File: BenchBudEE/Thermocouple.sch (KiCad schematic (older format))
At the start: 28 parts, among them P2 CONN_3X2, P3 CONN_2, U2 MCP3901, U3 LMT84, U4 OPA4170

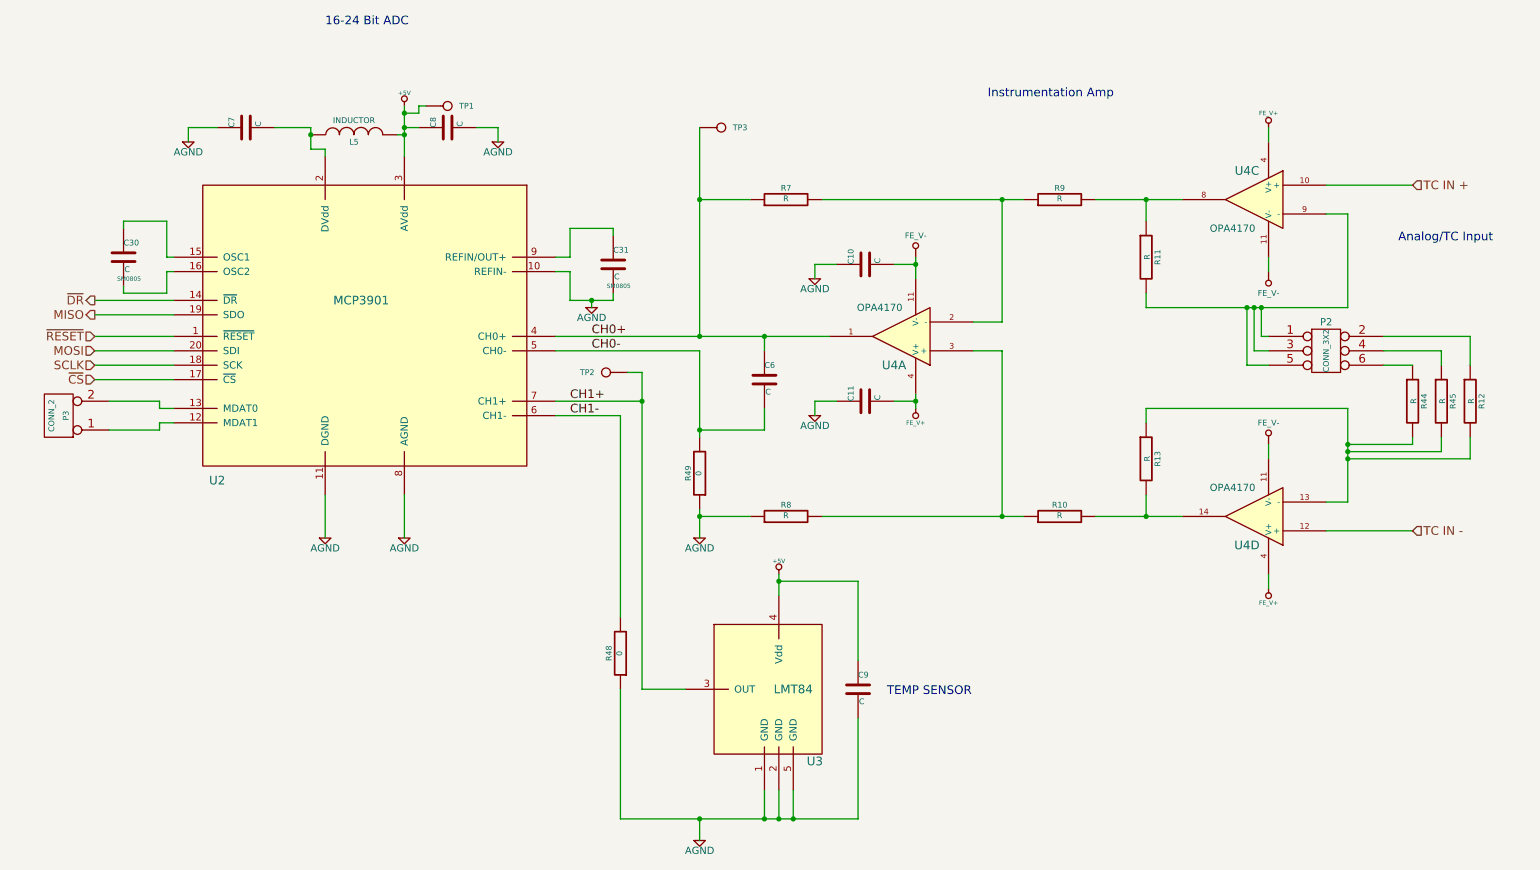
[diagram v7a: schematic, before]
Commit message: Analog IO Cleanup/Additions
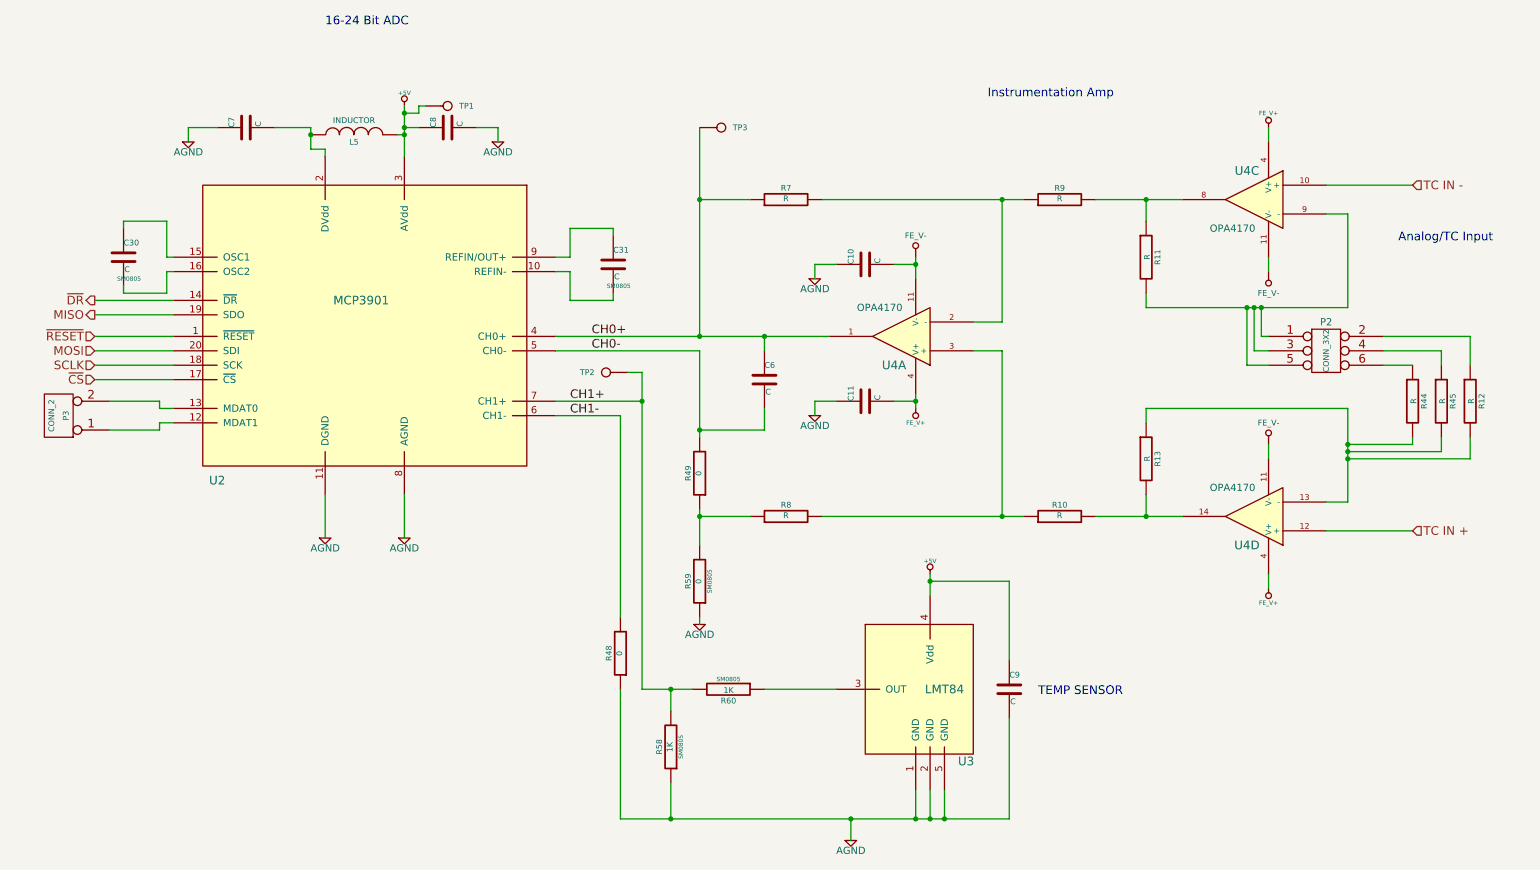
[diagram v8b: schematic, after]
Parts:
- added R58, R60: 1K, SM0805, symbol R
- added R59: 0, SM0805, symbol R
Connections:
- net AGND: now also R58.1, R59.1; no longer C31.2, R49.1, R8.1, U2.10 (REFIN-)
- net CH1+: now also R58.2, R60.2; no longer U3.3 (OUT)
- net TC IN +: now also U4.12 (+); no longer U4.10 (+)
- net TC IN -: now also U4.10 (+); no longer U4.12 (+)
- new net: R49.1, R59.2, R8.1
- new net: C31.2, U2.10 (REFIN-)
- new net: R60.1, U3.3 (OUT)
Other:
- moved on the sheet: C9, U3
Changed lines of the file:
@@
 Sheet 2 9
 Title ""
-Date "20 mar 2014"
+Date "26 mar 2014"
 Rev ""
 Comp ""
@@
 $EndDescr
 Text HLabel 10200 2100 2    60   Input ~ 0
+TC IN -
+Text HLabel 10200 4500 2    60   Input ~ 0
 TC IN +
-Text HLabel 10200 4500 2    60   Input ~ 0
-TC IN -
 Text HLabel 1050 3250 0    60   Input ~ 0
 MOSI
@@
 L LMT84 U3
 U 1 1 5303AA1C
-P 5700 5650
-F 0 "U3" H 6050 5200 60  0000 C CNN
-F 1 "LMT84" H 5900 5700 60  0000 C CNN
-F 2 "" H 6000 5500 60  0000 C CNN
-F 3 "" H 6000 5500 60  0000 C CNN
-	1    5700 5650
-	1    0    0    -1
-$EndComp
-$Comp
-L +5V #PWR9
+P 6750 5650
+F 0 "U3" H 7100 5200 60  0000 C CNN
+F 1 "LMT84" H 6950 5700 60  0000 C CNN
+F 2 "" H 7050 5500 60  0000 C CNN
+F 3 "" H 7050 5500 60  0000 C CNN
+	1    6750 5650
+	1    0    0    -1
+$EndComp
+$Comp
+L +5V #PWR01
 U 1 1 5303ACCB
-P 5800 4800
-F 0 "#PWR9" H 5800 4890 20  0001 C CNN
-F 1 "+5V" H 5800 4890 30  0000 C CNN
-F 2 "" H 5800 4800 60  0000 C CNN
-F 3 "" H 5800 4800 60  0000 C CNN
-	1    5800 4800
+P 6850 4800
+F 0 "#PWR01" H 6850 4890 20  0001 C CNN
+F 1 "+5V" H 6850 4890 30  0000 C CNN
+F 2 "" H 6850 4800 60  0000 C CNN
+F 3 "" H 6850 4800 60  0000 C CNN
+	1    6850 4800
 	1    0    0    -1
 $EndComp
@@
 L C C9
 U 1 1 5303AD83
-P 6350 5600
-F 0 "C9" H 6350 5700 40  0000 L CNN
-F 1 "C" H 6356 5515 40  0000 L CNN
-F 2 "~" H 6388 5450 30  0000 C CNN
-F 3 "~" H 6350 5600 60  0000 C CNN
-	1    6350 5600
+P 7400 5600
+F 0 "C9" H 7400 5700 40  0000 L CNN
+F 1 "C" H 7406 5515 40  0000 L CNN
+F 2 "~" H 7438 5450 30  0000 C CNN
+F 3 "~" H 7400 5600 60  0000 C CNN
+	1    7400 5600
 	1    0    0    -1
 $EndComp
@@
 $EndComp
 $Comp
-L +5V #PWR3
+L +5V #PWR02
 U 1 1 5303B53D
 P 3200 1550
-F 0 "#PWR3" H 3200 1640 20  0001 C CNN
+F 0 "#PWR02" H 3200 1640 20  0001 C CNN
 F 1 "+5V" H 3200 1640 30  0000 C CNN
 F 2 "" H 3200 1550 60  0000 C CNN
@@
 	0    -1   -1   0
 $EndComp
-Text Notes 6550 5650 0    60   ~ 0
+Text Notes 7600 5650 0    60   ~ 0
 TEMP SENSOR
 Text HLabel 1050 3150 0    60   Input ~ 0
@@
 Connection ~ 5250 4400
 Wire Wire Line
-	5250 6500 5250 6650
+	6300 6500 6300 6650
 Wire Wire Line
 	4250 3250 5250 3250
@@
 	4850 3400 4850 5600
 Wire Wire Line
-	4850 5600 5150 5600
-Wire Wire Line
 	4700 3700 4250 3700
 Wire Wire Line
-	4700 6500 6350 6500
-Wire Wire Line
-	5700 6500 5700 6300
-Wire Wire Line
-	5800 6500 5800 6300
-Connection ~ 5700 6500
-Wire Wire Line
-	5900 6500 5900 6300
-Connection ~ 5800 6500
-Wire Wire Line
-	5800 4800 5800 4950
-Wire Wire Line
-	5800 4850 6350 4850
-Wire Wire Line
-	6350 4850 6350 5400
-Connection ~ 5800 4850
-Wire Wire Line
-	6350 6500 6350 5800
-Connection ~ 5900 6500
-Connection ~ 5250 6500
+	4700 6500 7400 6500
+Wire Wire Line
+	6750 6500 6750 6300
+Wire Wire Line
+	6850 6500 6850 6300
+Connection ~ 6750 6500
+Wire Wire Line
+	6950 6500 6950 6300
+Connection ~ 6850 6500
+Wire Wire Line
+	6850 4800 6850 4950
+Wire Wire Line
+	6850 4850 7400 4850
+Wire Wire Line
+	7400 4850 7400 5400
+Connection ~ 6850 4850
+Wire Wire Line
+	7400 6500 7400 5800
+Connection ~ 6950 6500
+Connection ~ 6300 6500
 Wire Wire Line
 	6050 2750 6050 2650
@@
 	5250 3250 5250 3850
 Wire Wire Line
-	5250 4350 5250 4550
+	5250 4350 5250 4600
 Connection ~ 5250 3800
 Wire Wire Line
@@
 MISO
 $Comp
-L FE_V+ #PWR13
+L FE_V+ #PWR03
 U 1 1 5311A08F
 P 6750 3650
-F 0 "#PWR13" H 6750 3750 30  0001 C CNN
+F 0 "#PWR03" H 6750 3750 30  0001 C CNN
 F 1 "FE_V+" H 6750 3750 30  0000 C CNN
 F 2 "" H 6750 3650 60  0000 C CNN
@@
 $EndComp
 $Comp
-L FE_V+ #PWR17
+L FE_V+ #PWR04
 U 1 1 5311A095
 P 9200 4900
-F 0 "#PWR17" H 9200 5000 30  0001 C CNN
+F 0 "#PWR04" H 9200 5000 30  0001 C CNN
 F 1 "FE_V+" H 9200 5000 30  0000 C CNN
 F 2 "" H 9200 4900 60  0000 C CNN
@@
 $EndComp
 $Comp
-L FE_V+ #PWR14
+L FE_V+ #PWR05
 U 1 1 5311A09B
 P 9200 1700
-F 0 "#PWR14" H 9200 1800 30  0001 C CNN
+F 0 "#PWR05" H 9200 1800 30  0001 C CNN
 F 1 "FE_V+" H 9200 1800 30  0000 C CNN
 F 2 "" H 9200 1700 60  0000 C CNN
@@
 $EndComp
 $Comp
-L FE_V- #PWR12
+L FE_V- #PWR11
 U 1 1 5311A0AD
 P 6750 2600
-F 0 "#PWR12" H 6750 2800 40  0001 C CNN
+F 0 "#PWR11" H 6750 2800 40  0001 C CNN
 F 1 "FE_V-" H 6750 2750 40  0000 C CNN
 F 2 "~" H 6750 2600 60  0000 C CNN
@@
 $EndComp
 $Comp
-L AGND #PWR2
+L AGND #PWR06
 U 1 1 5313730A
 P 2650 4550
-F 0 "#PWR2" H 2650 4550 40  0001 C CNN
+F 0 "#PWR06" H 2650 4550 40  0001 C CNN
 F 1 "AGND" H 2650 4480 50  0000 C CNN
 F 2 "" H 2650 4550 60  0000 C CNN
@@
 $EndComp
 $Comp
-L AGND #PWR4
+L AGND #PWR07
 U 1 1 53137321
 P 3200 4550
-F 0 "#PWR4" H 3200 4550 40  0001 C CNN
+F 0 "#PWR07" H 3200 4550 40  0001 C CNN
 F 1 "AGND" H 3200 4480 50  0000 C CNN
 F 2 "" H 3200 4550 60  0000 C CNN
@@
 $EndComp
 $Comp
-L AGND #PWR1
+L AGND #PWR08
 U 1 1 5313732C
 P 1700 1800
-F 0 "#PWR1" H 1700 1800 40  0001 C CNN
+F 0 "#PWR08" H 1700 1800 40  0001 C CNN
 F 1 "AGND" H 1700 1730 50  0000 C CNN
 F 2 "" H 1700 1800 60  0000 C CNN
@@
 $EndComp
 $Comp
-L AGND #PWR5
+L AGND #PWR09
 U 1 1 5313733C
 P 3850 1800
-F 0 "#PWR5" H 3850 1800 40  0001 C CNN
+F 0 "#PWR09" H 3850 1800 40  0001 C CNN
 F 1 "AGND" H 3850 1730 50  0000 C CNN
 F 2 "" H 3850 1800 60  0000 C CNN
@@
 $EndComp
 $Comp
-L AGND #PWR10
+L AGND #PWR010
 U 1 1 53137342
 P 6050 2750
-F 0 "#PWR10" H 6050 2750 40  0001 C CNN
+F 0 "#PWR010" H 6050 2750 40  0001 C CNN
 F 1 "AGND" H 6050 2680 50  0000 C CNN
 F 2 "" H 6050 2750 60  0000 C CNN
@@
 $EndComp
 $Comp
-L AGND #PWR11
+L AGND #PWR011
 U 1 1 53137352
 P 6050 3700
-F 0 "#PWR11" H 6050 3700 40  0001 C CNN
+F 0 "#PWR011" H 6050 3700 40  0001 C CNN
 F 1 "AGND" H 6050 3630 50  0000 C CNN
 F 2 "" H 6050 3700 60  0000 C CNN
@@
 $EndComp
 $Comp
-L AGND #PWR7
+L AGND #PWR012
 U 1 1 53137362
-P 5250 4550
-F 0 "#PWR7" H 5250 4550 40  0001 C CNN
-F 1 "AGND" H 5250 4480 50  0000 C CNN
-F 2 "" H 5250 4550 60  0000 C CNN
-F 3 "" H 5250 4550 60  0000 C CNN
-	1    5250 4550
-	1    0    0    -1
-$EndComp
-$Comp
-L AGND #PWR8
+P 5250 5150
+F 0 "#PWR012" H 5250 5150 40  0001 C CNN
+F 1 "AGND" H 5250 5080 50  0000 C CNN
+F 2 "" H 5250 5150 60  0000 C CNN
+F 3 "" H 5250 5150 60  0000 C CNN
+	1    5250 5150
+	1    0    0    -1
+$EndComp
+$Comp
+L AGND #PWR013
 U 1 1 53137372
-P 5250 6650
-F 0 "#PWR8" H 5250 6650 40  0001 C CNN
-F 1 "AGND" H 5250 6580 50  0000 C CNN
-F 2 "" H 5250 6650 60  0000 C CNN
-F 3 "" H 5250 6650 60  0000 C CNN
-	1    5250 6650
+P 6300 6650
+F 0 "#PWR013" H 6300 6650 40  0001 C CNN
+F 1 "AGND" H 6300 6580 50  0000 C CNN
+F 2 "" H 6300 6650 60  0000 C CNN
+F 3 "" H 6300 6650 60  0000 C CNN
+	1    6300 6650
 	1    0    0    -1
 $EndComp
@@
 	4650 2900 4650 2850
 $Comp
-L AGND #PWR6
-U 1 1 532597F2
-P 4500 2950
-F 0 "#PWR6" H 4500 2950 40  0001 C CNN
-F 1 "AGND" H 4500 2880 50  0000 C CNN
-F 2 "" H 4500 2950 60  0000 C CNN
-F 3 "" H 4500 2950 60  0000 C CNN
-	1    4500 2950
-	1    0    0    -1
-$EndComp
-Wire Wire Line
-	4500 2950 4500 2900
-Connection ~ 4500 2900
-$Comp
 L CONN_1 TP3
 U 1 1 532B3628
@@
 	3300 1600 3200 1600
 Connection ~ 3200 1600
+$Comp
+L R R59
+U 1 1 53307C38
+P 5250 4850
+F 0 "R59" V 5330 4850 40  0000 C CNN
+F 1 "0" V 5257 4851 40  0000 C CNN
+F 2 "SM0805" V 5180 4850 30  0000 C CNN
+F 3 "~" H 5250 4850 30  0000 C CNN
+	1    5250 4850
+	-1   0    0    1
+$EndComp
+Wire Wire Line
+	5250 5100 5250 5150
+$Comp
+L R R60
+U 1 1 53307D8E
+P 5450 5600
+F 0 "R60" V 5530 5600 40  0000 C CNN
+F 1 "1K" V 5457 5601 40  0000 C CNN
+F 2 "SM0805" V 5380 5600 30  0000 C CNN
+F 3 "~" H 5450 5600 30  0000 C CNN
+	1    5450 5600
+	0    1    1    0
+$EndComp
+Wire Wire Line
+	4850 5600 5200 5600
+Wire Wire Line
+	5700 5600 6200 5600
+$Comp
+L R R58
+U 1 1 53307EBF
+P 5050 6000
+F 0 "R58" V 5130 6000 40  0000 C CNN
+F 1 "1K" V 5057 6001 40  0000 C CNN
+F 2 "SM0805" V 4980 6000 30  0000 C CNN
+F 3 "~" H 5050 6000 30  0000 C CNN
+	1    5050 6000
+	-1   0    0    1
+$EndComp
+Wire Wire Line
+	5050 5600 5050 5750
+Connection ~ 5050 5600
+Wire Wire Line
+	5050 6250 5050 6500
+Connection ~ 5050 6500
 $EndSCHEMATC
